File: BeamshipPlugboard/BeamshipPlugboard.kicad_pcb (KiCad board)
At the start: 2 copper layers, 165.3 x 49.1 mm, 6 parts, among them J1 BEAMSPRING PLUGBOARD COLUMNS, J2 BEAMSPRING PLUGBOARD ROWS, J7 Conn_01x34

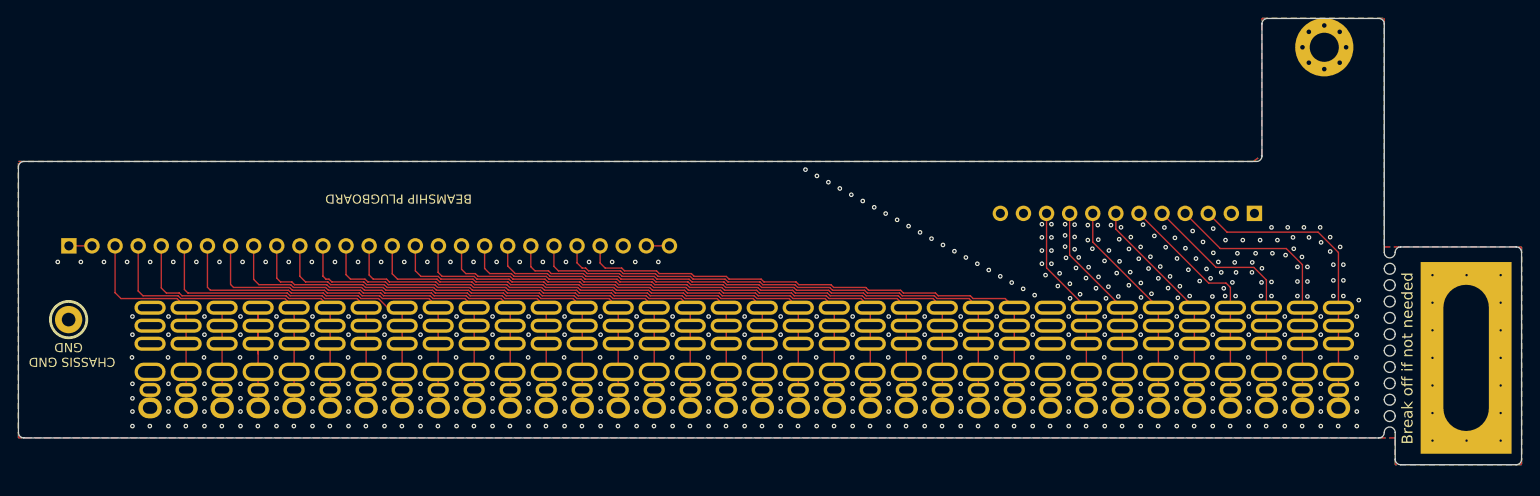
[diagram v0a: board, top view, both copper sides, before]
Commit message: Added locklights header, bumped revision
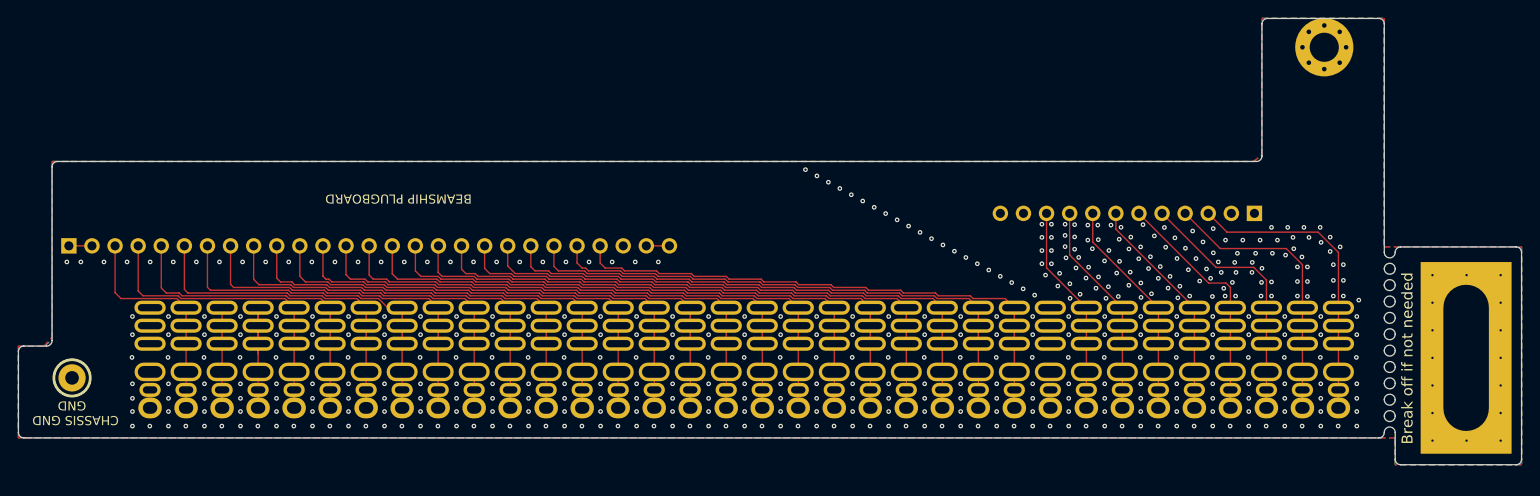
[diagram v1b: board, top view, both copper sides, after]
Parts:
- moved H3 6.42 mm to (90.6, 131.2)
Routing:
- net /BSGROUND: track 6.22 -> 5.12 mm
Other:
- outline, holes or cut-outs redrawn
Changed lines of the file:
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@@
   (general
     (thickness 1.6)
-    (drawings 71)
-    (tracks 899)
+    (drawings 75)
+    (tracks 898)
     (zones 0)
     (modules 6)
@@
     (0 F.Cu signal)
     (31 B.Cu signal)
-    (32 B.Adhes user)
-    (33 F.Adhes user)
-    (34 B.Paste user)
-    (35 F.Paste user)
+    (32 B.Adhes user hide)
+    (33 F.Adhes user hide)
+    (34 B.Paste user hide)
+    (35 F.Paste user hide)
     (36 B.SilkS user)
     (37 F.SilkS user)
-    (38 B.Mask user)
-    (39 F.Mask user)
+    (38 B.Mask user hide)
+    (39 F.Mask user hide)
     (40 Dwgs.User user hide)
     (41 Cmts.User user hide)
-    (42 Eco1.User user)
+    (42 Eco1.User user hide)
     (43 Eco2.User user hide)
     (44 Edge.Cuts user)
@@
     (pad_to_mask_clearance 0.0508)
     (solder_mask_min_width 0.101)
-    (aux_axis_origin 0 0)
+    (aux_axis_origin 84.7 137.8)
     (visible_elements 7FFFFF7F)
     (pcbplotparams
@@
       (viasonmask false)
       (mode 1)
-      (useauxorigin false)
+      (useauxorigin true)
       (hpglpennumber 1)
       (hpglpenspeed 20)
@@
       (outputformat 1)
       (mirror false)
-      (drillshape 1)
+      (drillshape 0)
       (scaleselection 1)
-      (outputdirectory ""))
+      (outputdirectory "gerbers"))
   )
   (net 0 "")
@@
   )
   (module TH-XWhatsIt:ChassisGnd (layer F.Cu)
-    (at 90.2208 124.7902)
+    (at 90.6 131.2)
     (descr "Mounting Hole 2.2mm, M2")
     (tags "mounting hole 2.2mm m2")
@@
     )
   )
+  (gr_line (start 87.79947 127.7) (end 85.3 127.7) (layer Edge.Cuts) (width 0.05))
+  (gr_line (start 88.39947 108) (end 88.39947 127.1) (layer Edge.Cuts) (width 0.05))
+  (gr_arc (start 87.79947 127.1) (end 87.79947 127.7) (angle -90) (layer Edge.Cuts) (width 0.05))
+  (gr_arc (start 85.3 128.3) (end 85.3 127.7) (angle -90) (layer Edge.Cuts) (width 0.05))
   (gr_text "Break off if not needed" (at 237.45 129.05 90) (layer F.SilkS)
     (effects (font (size 1.2 1.2) (thickness 0.3)))
@@
   (gr_arc (start 222.05 92.272852) (end 222.05 91.672852) (angle -90) (layer Edge.Cuts) (width 0.05))
   (gr_arc (start 220.85 106.8) (end 220.85 107.4) (angle -90) (layer Edge.Cuts) (width 0.05))
-  (gr_text "The left side must also be cut off, because the beamship uses 2x30 pin connectors, and this pluboard doesn't have the full width. (Note: there are two dummy pins in-between)" (at 157.75 109.78 180) (layer B.SilkS)
+  (gr_text "The left side must also be cut off, because the beamship uses 2x30 pin connectors, and this pluboard doesn't have the full width. (Note: there are two dummy pins in-between)" (at 158.75 109.78 180) (layer B.SilkS)
     (effects (font (size 1 1) (thickness 0.15)) (justify mirror))
   )
-  (gr_text "The right side of modern connectors must be cut off in order to not interfere with the mounting plate." (at 128.43 112.17 180) (layer B.SilkS)
+  (gr_text "The right side of modern connectors must be cut off in order to not interfere with the mounting plate." (at 129.43 112.17 180) (layer B.SilkS)
     (effects (font (size 1 1) (thickness 0.15)) (justify mirror))
   )
@@
     (effects (font (size 1 1) (thickness 0.15)) (justify mirror))
   )
-  (gr_text "CHASSIS\nGND" (at 90.35 128.6 180) (layer B.SilkS)
+  (gr_text "CHASSIS\nGND" (at 91 127.8 180) (layer B.SilkS)
     (effects (font (size 1 1) (thickness 0.15)) (justify mirror))
   )
@@
   (gr_arc (start 234.3 137.2) (end 234.3 137.8) (angle -90) (layer Edge.Cuts) (width 0.05))
   (gr_arc (start 85.3 137.2) (end 84.7 137.2) (angle -90) (layer Edge.Cuts) (width 0.05))
-  (gr_arc (start 85.3 108) (end 85.3 107.4) (angle -90) (layer Edge.Cuts) (width 0.05))
+  (gr_arc (start 88.99947 108) (end 88.99947 107.4) (angle -90) (layer Edge.Cuts) (width 0.05))
   (gr_arc (start 234.3 92.272852) (end 234.9 92.272852) (angle -90) (layer Edge.Cuts) (width 0.05))
   (gr_arc (start 67.270369 91.082889) (end 67.270369 91.678202) (angle -180) (layer Cmts.User) (width 0.05))
@@
   )
   (gr_line (start 234.9 117.4) (end 234.9 92.272852) (layer Edge.Cuts) (width 0.05))
-  (gr_line (start 85.3 107.4) (end 220.85 107.4) (layer Edge.Cuts) (width 0.05))
-  (gr_line (start 84.7 137.2) (end 84.7 108) (layer Edge.Cuts) (width 0.05))
+  (gr_line (start 88.99947 107.4) (end 220.85 107.4) (layer Edge.Cuts) (width 0.05))
+  (gr_line (start 84.7 137.2) (end 84.7 128.3) (layer Edge.Cuts) (width 0.05))
   (gr_line (start 234.3 137.8) (end 85.3 137.8) (layer Edge.Cuts) (width 0.05))
   (dimension 5.003864 (width 0.3) (layer Dwgs.User)
@@
   (via (at 240.2 122.933333) (size 0.508) (drill 0.254) (layers F.Cu B.Cu) (net 1))
   (via (at 240.2 119.9) (size 0.508) (drill 0.254) (layers F.Cu B.Cu) (net 1))
-  (segment (start 91.0013 125.5707) (end 90.2208 124.7902) (width 0.1524) (layer F.Cu) (net 1))
   (segment (start 90.2208 116.709355) (end 90.24947 116.680685) (width 0.1524) (layer F.Cu) (net 1))
   (segment (start 90.24947 116.680685) (end 92.78947 116.680685) (width 0.1524) (layer F.Cu) (net 1))
@@
   (via (at 94.11 118.45) (size 0.508) (drill 0.254) (layers F.Cu B.Cu) (net 1))
   (via (at 91.57 118.45) (size 0.508) (drill 0.254) (layers F.Cu B.Cu) (net 1))
-  (via (at 89.03 118.45) (size 0.508) (drill 0.254) (layers F.Cu B.Cu) (net 1))
+  (via (at 90.03 118.45) (size 0.508) (drill 0.254) (layers F.Cu B.Cu) (net 1))
   (via (at 149.99 118.45) (size 0.508) (drill 0.254) (layers F.Cu B.Cu) (net 1))
   (via (at 152.53 118.45) (size 0.508) (drill 0.254) (layers F.Cu B.Cu) (net 1))
@@
     (polygon
       (pts
-        (xy 84.7 107.4) (xy 220.5 107.4) (xy 221.45 106.7) (xy 221.45 91.65) (xy 234.9 91.65)
-        (xy 234.9 116.8) (xy 250 116.8) (xy 250 140.75) (xy 236.1 140.75) (xy 236.1 137.8)
-        (xy 234.9 137.8) (xy 84.7 137.8)
+        (xy 84.7 127.7) (xy 87.5 127.7) (xy 88.4 126.7) (xy 88.4 107.4) (xy 220.5 107.4)
+        (xy 221.45 106.7) (xy 221.45 91.65) (xy 234.9 91.65) (xy 234.9 116.8) (xy 250 116.8)
+        (xy 250 140.75) (xy 236.1 140.75) (xy 236.1 137.8) (xy 234.9 137.8) (xy 84.7 137.8)
       )
     )
@@
       (pts
         (xy 234.9 116.8) (xy 250 116.8) (xy 250 140.75) (xy 236.1 140.75) (xy 236.1 137.8)
-        (xy 84.7 137.8) (xy 84.7 107.4) (xy 220.5 107.4) (xy 221.45 106.7) (xy 221.45 91.65)
-        (xy 234.9 91.65)
+        (xy 84.7 137.8) (xy 84.7 127.7) (xy 87.6 127.7) (xy 88.4 127) (xy 88.4 107.4)
+        (xy 220.5 107.4) (xy 221.45 106.7) (xy 221.45 91.65) (xy 234.9 91.65)
       )
     )

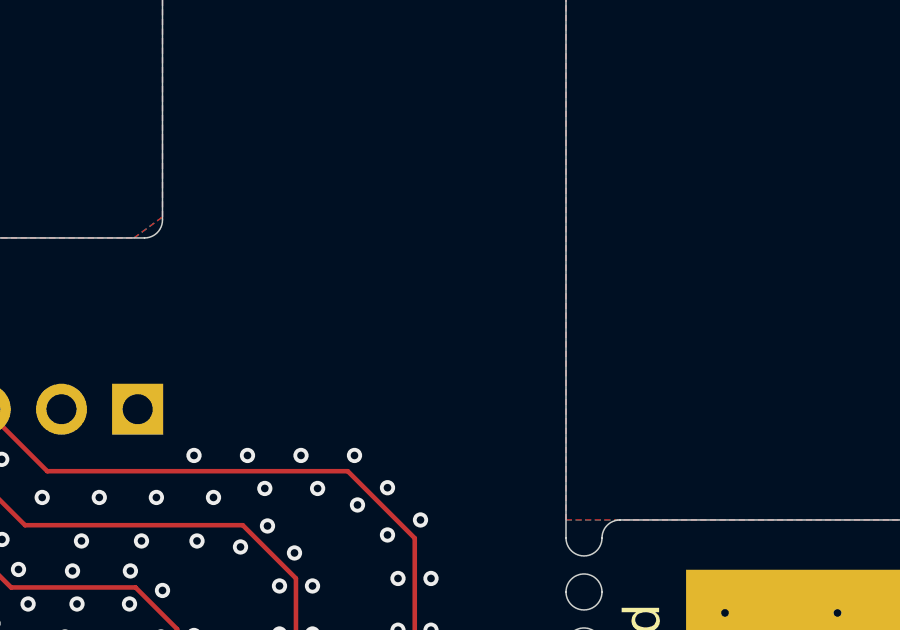
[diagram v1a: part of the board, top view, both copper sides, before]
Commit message: Beamship Plugboard: added extra grounding hole.
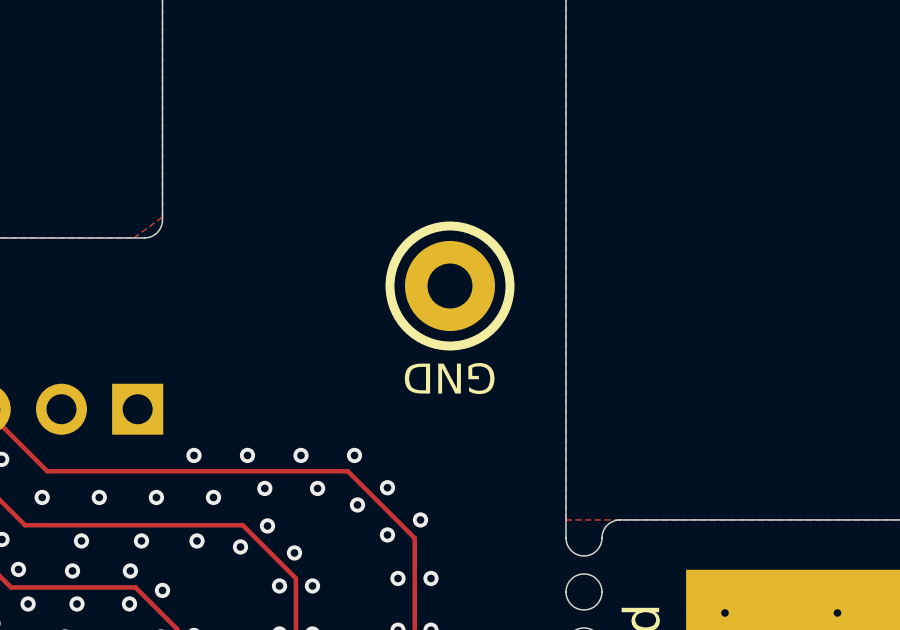
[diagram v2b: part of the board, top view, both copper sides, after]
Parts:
- added H4: GROUND STRAP, TH-XWhatsIt:ChassisGnd, F.Cu at (231.0, 109.0)
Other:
- board text added: "GND"
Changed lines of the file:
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@@
   (general
     (thickness 1.6)
-    (drawings 75)
+    (drawings 76)
     (tracks 898)
     (zones 0)
-    (modules 6)
+    (modules 7)
     (nets 35)
   )
@@
     (add_net "Net-(J7-Pad4)")
   )
+  (module TH-XWhatsIt:ChassisGnd (layer F.Cu)
+    (at 231.03332 109.00156)
+    (descr "Mounting Hole 2.2mm, M2")
+    (tags "mounting hole 2.2mm m2")
+    (attr virtual)
+    (fp_text reference H4 (at 0 -3.2) (layer F.SilkS) hide
+      (effects (font (size 1 1) (thickness 0.15)))
+    )
+    (fp_text value "GROUND STRAP" (at 0 2.6) (layer F.Fab) hide
+      (effects (font (size 1 1) (thickness 0.15)))
+    )
+    (fp_text user GND (at -0.0127 3.048 180 unlocked) (layer F.SilkS)
+      (effects (font (size 1 1) (thickness 0.15)))
+    )
+    (fp_text user GND (at 2.7178 -2.4257) (layer F.SilkS) hide
+      (effects (font (size 1 1) (thickness 0.15)))
+    )
+    (fp_text user %R (at 0.3 0) (layer F.Fab)
+      (effects (font (size 1 1) (thickness 0.15)))
+    )
+    (fp_circle (center 0 0) (end 1.6 0) (layer F.CrtYd) (width 0.05))
+    (fp_circle (center 0 0) (end 2.2 0) (layer Cmts.User) (width 0.15))
+    (fp_circle (center 0 0) (end 2 0) (layer F.SilkS) (width 0.3))
+    (pad 1 thru_hole circle (at 0 0) (size 3 3) (drill 1.5) (layers *.Cu *.Mask)
+      (net 1 /BSGROUND))
+  )
   (module TH-XWhatsIt:beamship_mounting_hole (layer F.Cu)
     (at 243.903489 129)
@@
       (effects (font (size 1 1) (thickness 0.15)))
     )
+    (fp_circle (center 0 0) (end 3.2 0) (layer Cmts.User) (width 0.15))
     (fp_circle (center 0 0) (end 3.45 0) (layer F.CrtYd) (width 0.05))
-    (fp_circle (center 0 0) (end 3.2 0) (layer Cmts.User) (width 0.15))
     (fp_text user %R (at 0.3 0) (layer F.Fab)
       (effects (font (size 1 1) (thickness 0.15)))
@@
       (effects (font (size 1 1) (thickness 0.15)))
     )
+    (fp_circle (center 0 0) (end 2 0) (layer F.SilkS) (width 0.3))
+    (fp_circle (center 0 0) (end 2.2 0) (layer Cmts.User) (width 0.15))
     (fp_circle (center 0 0) (end 1.6 0) (layer F.CrtYd) (width 0.05))
-    (fp_circle (center 0 0) (end 2.2 0) (layer Cmts.User) (width 0.15))
-    (fp_circle (center 0 0) (end 2 0) (layer F.SilkS) (width 0.3))
     (fp_text user "CHASSIS GND" (at 0.3792 4.6598 180 unlocked) (layer F.SilkS)
       (effects (font (size 1 1) (thickness 0.15)))
@@
       (effects (font (size 1 1) (thickness 0.15)) (justify mirror))
     )
+    (fp_line (start -1.8 -67.8) (end -1.8 1.8) (layer B.CrtYd) (width 0.05))
+    (fp_line (start 1.75 -67.8) (end -1.8 -67.8) (layer B.CrtYd) (width 0.05))
+    (fp_line (start 1.75 1.8) (end 1.75 -67.8) (layer B.CrtYd) (width 0.05))
+    (fp_line (start -1.8 1.8) (end 1.75 1.8) (layer B.CrtYd) (width 0.05))
+    (fp_line (start 0 1.33) (end 1.33 1.33) (layer B.SilkS) (width 0.12))
+    (fp_line (start 1.33 1.33) (end 1.33 0) (layer B.SilkS) (width 0.12))
+    (fp_line (start 1.33 -1.27) (end 1.33 -67.37) (layer B.SilkS) (width 0.12))
+    (fp_line (start -1.33 -67.37) (end 1.33 -67.37) (layer B.SilkS) (width 0.12))
+    (fp_line (start -1.33 -1.27) (end -1.33 -67.37) (layer B.SilkS) (width 0.12))
+    (fp_line (start -1.33 -1.27) (end 1.33 -1.27) (layer B.SilkS) (width 0.12))
+    (fp_line (start -1.27 -67.31) (end -1.27 1.27) (layer B.Fab) (width 0.1))
+    (fp_line (start 1.27 -67.31) (end -1.27 -67.31) (layer B.Fab) (width 0.1))
+    (fp_line (start 1.27 0.635) (end 1.27 -67.31) (layer B.Fab) (width 0.1))
+    (fp_line (start 0.635 1.27) (end 1.27 0.635) (layer B.Fab) (width 0.1))
     (fp_line (start -1.27 1.27) (end 0.635 1.27) (layer B.Fab) (width 0.1))
-    (fp_line (start 0.635 1.27) (end 1.27 0.635) (layer B.Fab) (width 0.1))
-    (fp_line (start 1.27 0.635) (end 1.27 -67.31) (layer B.Fab) (width 0.1))
-    (fp_line (start 1.27 -67.31) (end -1.27 -67.31) (layer B.Fab) (width 0.1))
-    (fp_line (start -1.27 -67.31) (end -1.27 1.27) (layer B.Fab) (width 0.1))
-    (fp_line (start -1.33 -1.27) (end 1.33 -1.27) (layer B.SilkS) (width 0.12))
-    (fp_line (start -1.33 -1.27) (end -1.33 -67.37) (layer B.SilkS) (width 0.12))
-    (fp_line (start -1.33 -67.37) (end 1.33 -67.37) (layer B.SilkS) (width 0.12))
-    (fp_line (start 1.33 -1.27) (end 1.33 -67.37) (layer B.SilkS) (width 0.12))
-    (fp_line (start 1.33 1.33) (end 1.33 0) (layer B.SilkS) (width 0.12))
-    (fp_line (start 0 1.33) (end 1.33 1.33) (layer B.SilkS) (width 0.12))
-    (fp_line (start -1.8 1.8) (end 1.75 1.8) (layer B.CrtYd) (width 0.05))
-    (fp_line (start 1.75 1.8) (end 1.75 -67.8) (layer B.CrtYd) (width 0.05))
-    (fp_line (start 1.75 -67.8) (end -1.8 -67.8) (layer B.CrtYd) (width 0.05))
-    (fp_line (start -1.8 -67.8) (end -1.8 1.8) (layer B.CrtYd) (width 0.05))
     (fp_text user %R (at 0 -33.02 180) (layer B.Fab)
       (effects (font (size 1 1) (thickness 0.15)) (justify mirror))
@@
       (effects (font (size 1 1) (thickness 0.15)) (justify mirror))
     )
+    (fp_line (start -1.8 -29.7) (end -1.8 1.8) (layer B.CrtYd) (width 0.05))
+    (fp_line (start 1.75 -29.7) (end -1.8 -29.7) (layer B.CrtYd) (width 0.05))
+    (fp_line (start 1.75 1.8) (end 1.75 -29.7) (layer B.CrtYd) (width 0.05))
+    (fp_line (start -1.8 1.8) (end 1.75 1.8) (layer B.CrtYd) (width 0.05))
+    (fp_line (start 0 1.33) (end 1.33 1.33) (layer B.SilkS) (width 0.12))
+    (fp_line (start 1.33 1.33) (end 1.33 0) (layer B.SilkS) (width 0.12))
+    (fp_line (start 1.33 -1.27) (end 1.33 -29.27) (layer B.SilkS) (width 0.12))
+    (fp_line (start -1.33 -29.27) (end 1.33 -29.27) (layer B.SilkS) (width 0.12))
+    (fp_line (start -1.33 -1.27) (end -1.33 -29.27) (layer B.SilkS) (width 0.12))
+    (fp_line (start -1.33 -1.27) (end 1.33 -1.27) (layer B.SilkS) (width 0.12))
+    (fp_line (start -1.27 -29.21) (end -1.27 1.27) (layer B.Fab) (width 0.1))
+    (fp_line (start 1.27 -29.21) (end -1.27 -29.21) (layer B.Fab) (width 0.1))
+    (fp_line (start 1.27 0.635) (end 1.27 -29.21) (layer B.Fab) (width 0.1))
+    (fp_line (start 0.635 1.27) (end 1.27 0.635) (layer B.Fab) (width 0.1))
     (fp_line (start -1.27 1.27) (end 0.635 1.27) (layer B.Fab) (width 0.1))
-    (fp_line (start 0.635 1.27) (end 1.27 0.635) (layer B.Fab) (width 0.1))
-    (fp_line (start 1.27 0.635) (end 1.27 -29.21) (layer B.Fab) (width 0.1))
-    (fp_line (start 1.27 -29.21) (end -1.27 -29.21) (layer B.Fab) (width 0.1))
-    (fp_line (start -1.27 -29.21) (end -1.27 1.27) (layer B.Fab) (width 0.1))
-    (fp_line (start -1.33 -1.27) (end 1.33 -1.27) (layer B.SilkS) (width 0.12))
-    (fp_line (start -1.33 -1.27) (end -1.33 -29.27) (layer B.SilkS) (width 0.12))
-    (fp_line (start -1.33 -29.27) (end 1.33 -29.27) (layer B.SilkS) (width 0.12))
-    (fp_line (start 1.33 -1.27) (end 1.33 -29.27) (layer B.SilkS) (width 0.12))
-    (fp_line (start 1.33 1.33) (end 1.33 0) (layer B.SilkS) (width 0.12))
-    (fp_line (start 0 1.33) (end 1.33 1.33) (layer B.SilkS) (width 0.12))
-    (fp_line (start -1.8 1.8) (end 1.75 1.8) (layer B.CrtYd) (width 0.05))
-    (fp_line (start 1.75 1.8) (end 1.75 -29.7) (layer B.CrtYd) (width 0.05))
-    (fp_line (start 1.75 -29.7) (end -1.8 -29.7) (layer B.CrtYd) (width 0.05))
-    (fp_line (start -1.8 -29.7) (end -1.8 1.8) (layer B.CrtYd) (width 0.05))
     (fp_text user %R (at 0 -13.97) (layer B.Fab)
       (effects (font (size 1 1) (thickness 0.15)) (justify mirror))
@@
     )
   )
+  (gr_text GND (at 231.05364 112.06988 180) (layer B.SilkS)
+    (effects (font (size 1 1) (thickness 0.15)) (justify mirror))
+  )
   (gr_line (start 87.79947 127.7) (end 85.3 127.7) (layer Edge.Cuts) (width 0.05))
